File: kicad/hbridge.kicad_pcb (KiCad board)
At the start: 2 copper layers, 50 x 50 mm, 33 parts, among them P1 CONN_01X01, P10 CONN_01X01, P11 CONN_01X02, P2 CONN_01X01, P3 CONN_01X01, P4 CONN_01X01, P5 CONN_01X01, P6 CONN_01X02, P7 CONN_01X01, P8 CONN_01X01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

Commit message: wip #1
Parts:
- C2, C4: footprint Capacitors_SMD:C_0805 -> Capacitors_Tantalum_SMD:TantalC_SizeB_EIA-3528_HandSoldering
- D1, D2: footprint Diodes_ThroughHole:Diode_DO-35_SOD27_Horizontal_RM10 -> Diodes_SMD:Diode-DO-214BA
- P11, P6: footprint Socket_Strips:Socket_Strip_Straight_1x02 -> Connect:AK300-2
- moved C4 63.1 mm to (144.8, 83.8), turned to 90 degrees
- moved P11 50.4 mm to (129.5, 53.3)
- moved C6 48.2 mm to (114.3, 50.8)
- moved C7 47.7 mm to (111.8, 53.3)
- moved P5 47.1 mm to (139.7, 96.5)
- moved P2 46.7 mm to (134.6, 96.5)
- moved P1 45.3 mm to (115.0, 95.0)
- moved P4 45.0 mm to (120.0, 95.0)
- moved P3 39.6 mm to (124.5, 91.4)
- moved P10 38.3 mm to (104.1, 58.4)
- moved C2 38.1 mm to (116.8, 76.2)
- moved C5 37.7 mm to (109.2, 58.4)
- moved U3 35.4 mm to (119.4, 55.9), turned to 180 degrees
- moved C3 30.4 mm to (120.0, 90.0), turned to 270 degrees
- moved R5 29.4 mm to (111.8, 55.9), turned to 90 degrees
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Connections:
- net /Half Bridge/GND renamed /Half Bridge 1/GND
- net /Half Bridge/OUT renamed /Half Bridge 2/OUT
- net /Half Bridge/VCC renamed /Half Bridge 1/VCC
- net /Half Bridge/VPP renamed /Half Bridge 1/VPP
- net /Half Bridge/~SD renamed /Half Bridge 1/~SD
- D1 pad 2: Net-(D1-Pad2) -> Net-(C2-Pad1)
- D2 pad 2: Net-(D2-Pad2) -> Net-(C4-Pad1)
- P2 pad 1: /Half Bridge/IN -> /Half Bridge 1/IN
- P5 pad 1: /Half Bridge/IN -> /Half Bridge 2/IN
- U1 pad 2: /Half Bridge/IN -> /Half Bridge 1/IN
- U1 pad 8: Net-(D1-Pad2) -> Net-(C2-Pad1)
- U2 pad 2: /Half Bridge/IN -> /Half Bridge 2/IN
- U2 pad 8: Net-(D2-Pad2) -> Net-(C4-Pad1)
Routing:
- net /Half Bridge 1/GND: track 0.00 -> 84.6 mm
- net /Half Bridge 1/VPP: track 0.00 -> 36.2 mm
- net /Current Sensor/IP+: track 0.00 -> 21.6 mm
- net /Half Bridge 1/~SD: track 0.00 -> 18.0 mm
- net /Half Bridge 2/OUT: track 0.00 -> 15.3 mm
- net Net-(Q2-Pad2): track 0.00 -> 12.8 mm
- net Net-(Q4-Pad2): track 0.00 -> 12.8 mm
- net /Current Sensor/IP-: track 0.00 -> 9.32 mm
- net Net-(Q3-Pad2): track 0.00 -> 6.67 mm
- net Net-(Q1-Pad2): track 0.00 -> 6.67 mm
- net Net-(R4-Pad2): track 0.00 -> 4.93 mm
- net Net-(R3-Pad2): track 0.00 -> 4.93 mm

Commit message: initial place & route
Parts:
- P6: moved to B.Cu
- moved P8 44.1 mm to (113.0, 96.5)
- moved P9 43.2 mm to (108.0, 96.5)
- moved P7 40.8 mm to (102.9, 96.5)
- moved P10 40.6 mm to (118.1, 96.5)
- moved C7 38.3 mm to (115.6, 91.4), turned to 180 degrees
- moved R6 36.7 mm to (105.4, 91.4), turned to 0 degrees
- moved R5 32.7 mm to (119.4, 87.6)
- moved C3 23.5 mm to (143.5, 89.4), turned to 0 degrees
- moved P3 18.5 mm to (142.2, 96.5)
- moved P6 15.2 mm to (109.0, 53.6), turned to 180 degrees
- moved C2 15.2 mm to (131.8, 78.5)
- moved C1 15.0 mm to (131.8, 89.4), turned to 0 degrees
- moved C5 12.8 mm to (121.4, 54.6), turned to 90 degrees
- moved P4 12.2 mm to (132.1, 96.5)
- moved P1 12.1 mm to (127.0, 96.5)
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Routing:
- net /Current Sensor/~FAULT: track 0.00 -> 67.2 mm
- net GNDA: track 0.00 -> 64.8 mm
- net /Current Sensor/AVCC: track 0.00 -> 62.9 mm, vias 0 -> 1
- net Net-(R5-Pad2): track 0.00 -> 36.5 mm
- net /Half Bridge 1/VCC: track 0.00 -> 34.1 mm
- net /Half Bridge 1/GND: track 84.6 -> 64.5 mm
- net /Half Bridge 2/OUT: track 15.3 -> 33.6 mm
- net /Half Bridge 1/IN: track 0.00 -> 16.7 mm
- net /Half Bridge 2/IN: track 0.00 -> 16.3 mm
- net /Current Sensor/VOUT: track 0.00 -> 10.7 mm
- net /Current Sensor/IP+: track 21.6 -> 32.1 mm
- net Net-(C4-Pad1): track 0.00 -> 7.06 mm
- net Net-(Q2-Pad2): track 12.8 -> 5.77 mm
- net Net-(Q4-Pad2): track 12.8 -> 5.80 mm
- net Net-(C2-Pad1): track 0.00 -> 6.84 mm
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
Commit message: PCB good
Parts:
- moved R6 15.9 mm to (121.3, 91.4)
- moved P7 14.0 mm to (116.8, 96.5)
- moved P9 14.0 mm to (121.9, 96.5)
- moved R5 7.62 mm to (111.8, 87.6)
- moved P10 6.35 mm to (111.8, 96.5)
- moved P8 6.35 mm to (106.7, 96.5)
- moved P2 5.08 mm to (132.1, 96.5)
- moved P4 5.08 mm to (137.2, 96.5)
- moved C7 4.81 mm to (110.8, 91.4)
- moved C3 4.34 mm to (145.0, 93.5)
- moved U1 4.33 mm to (132.7, 88.1)
- moved U2 4.32 mm to (144.4, 88.1)
- moved C1 4.07 mm to (132.1, 93.5)
- moved R3 3.95 mm to (140.7, 77.5)
- moved C4 3.39 mm to (143.8, 81.3)
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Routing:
- net GNDA: track 64.8 -> 0.63 mm
- net /Half Bridge 1/GND: track 64.5 -> 19.4 mm, vias 0 -> 1
- net /Half Bridge 1/VPP: track 38.6 -> 0.00 mm
- net /Current Sensor/~FAULT: track 67.2 -> 50.4 mm
- net /Half Bridge 1/~SD: track 11.2 -> 22.6 mm
- net /Half Bridge 1/IN: track 16.7 -> 5.68 mm
- net Net-(R2-Pad2): track 0.00 -> 10.6 mm
- net /Current Sensor/IP-: track 8.78 -> 0.18 mm
- net Net-(Q1-Pad2): track 11.1 -> 19.3 mm
- net Net-(R5-Pad2): track 36.5 -> 43.7 mm
- net Net-(Q3-Pad2): track 11.1 -> 18.1 mm
- net /Current Sensor/AVCC: track 62.9 -> 59.4 mm
- net /Half Bridge 2/OUT: track 33.6 -> 30.2 mm
- net Net-(C4-Pad1): track 7.06 -> 10.3 mm
- net Net-(C2-Pad1): track 6.84 -> 10.0 mm
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- added copper zone on F.Cu, net /Current Sensor/IP+
- added copper zone on F.Cu, net /Current Sensor/IP-
- added copper zone on B.Cu, net /Half Bridge 1/GND
- added copper zone on B.Cu, net /Half Bridge 1/VPP
- added copper zone on F.Cu, net /Half Bridge 2/OUT
- added copper zone on F.Cu, net GNDA
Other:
- net class power added: clearance 0.2, trace_width 0.75, via_dia 1, via_drill 0.8

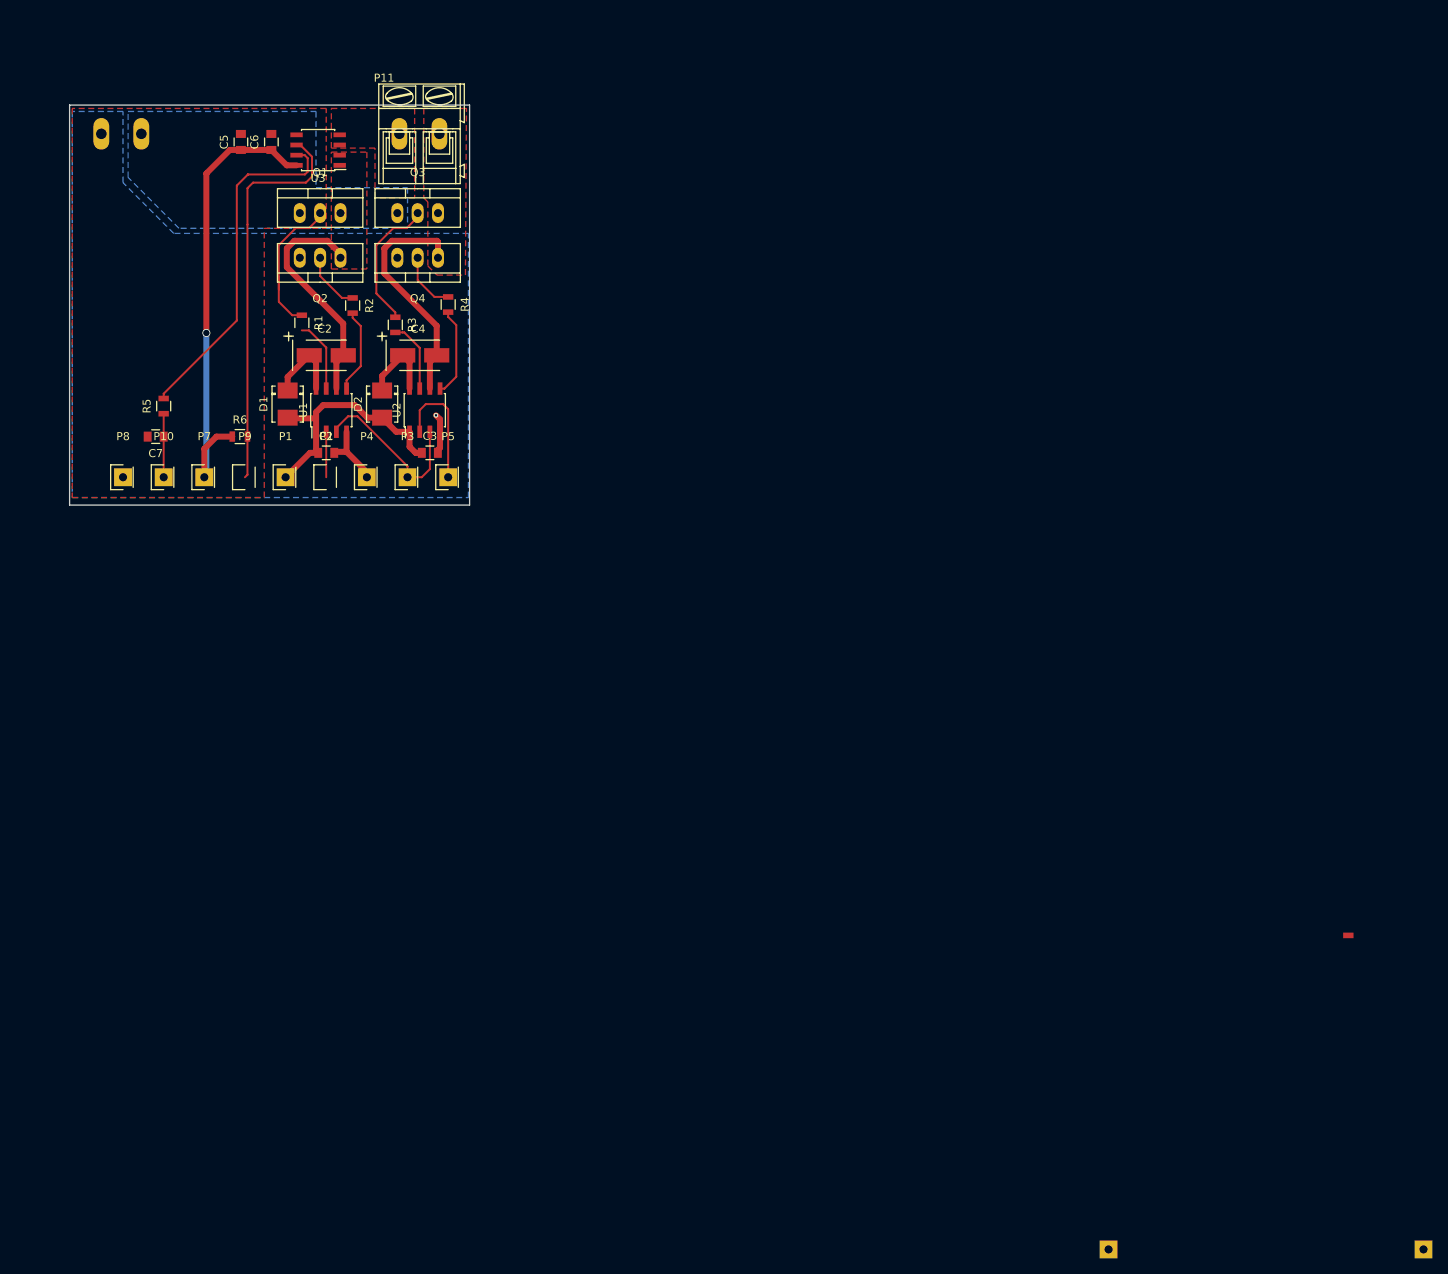
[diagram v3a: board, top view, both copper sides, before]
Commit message: add big cap for vpp
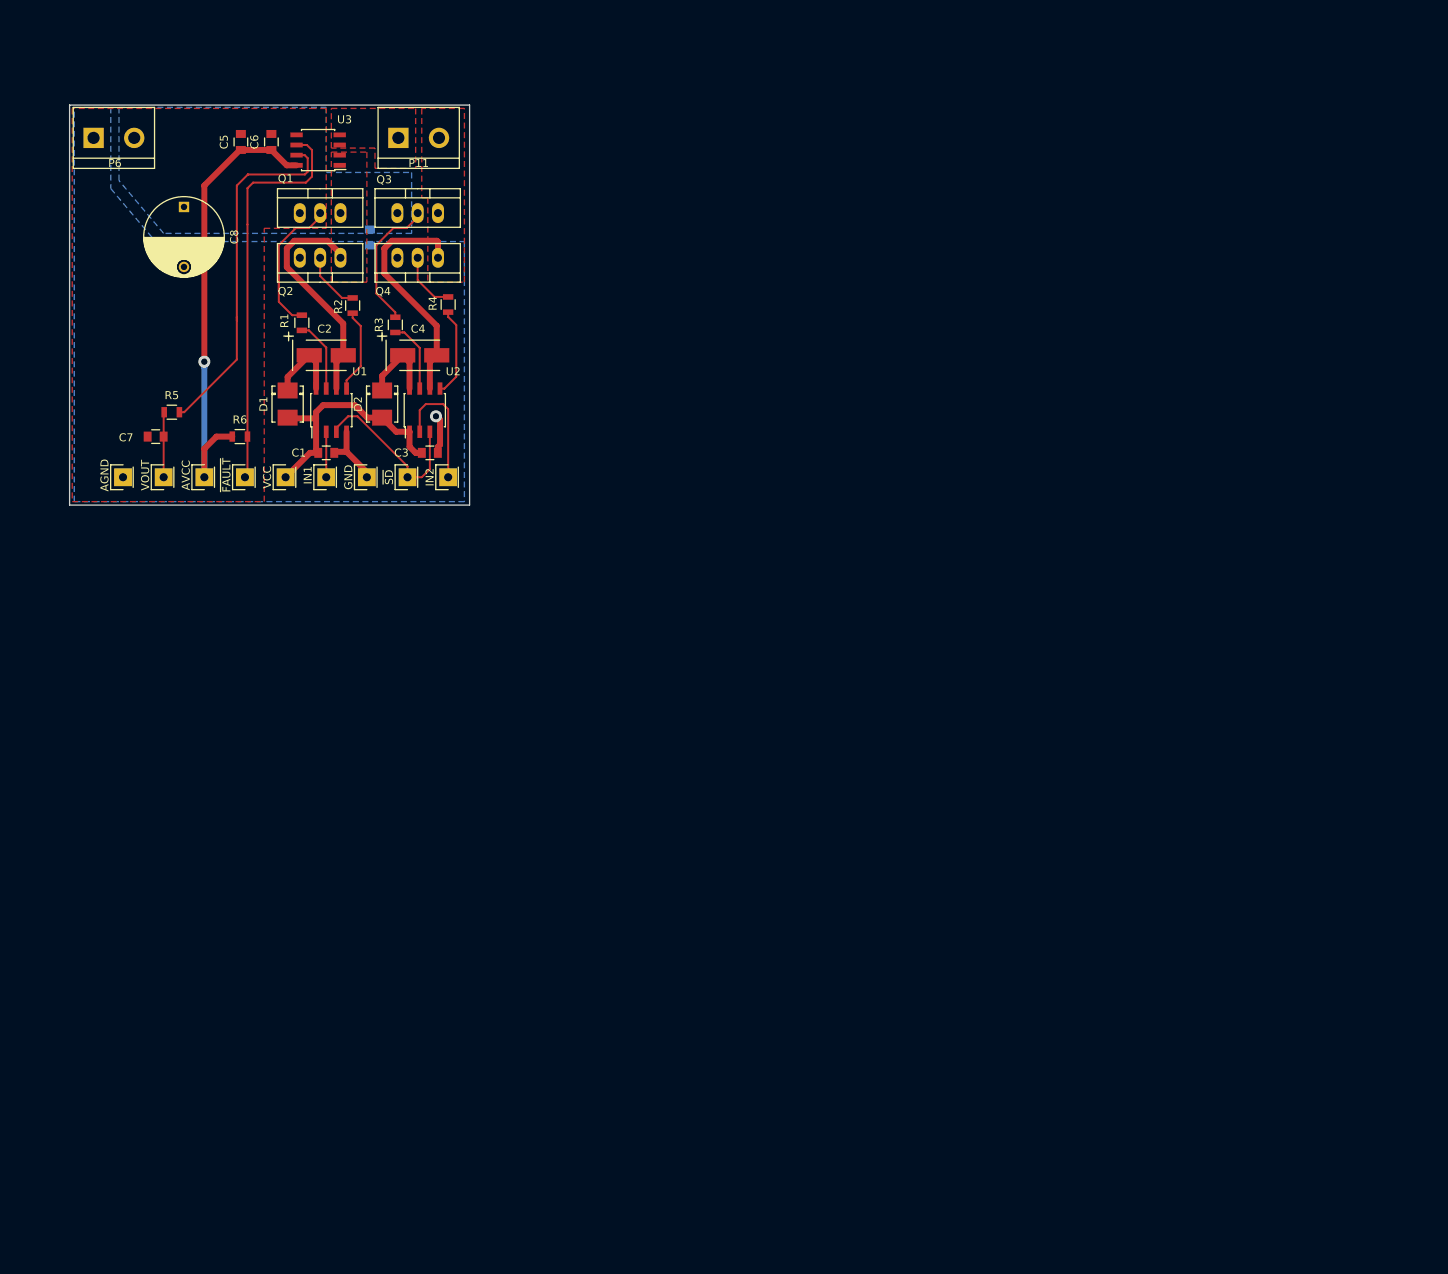
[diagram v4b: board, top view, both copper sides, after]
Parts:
- added C8: CP, Capacitors_ThroughHole:C_Radial_D10_L20_P7.5, F.Cu at (114.3, 62.7)
- added C9: C, Capacitors_SMD:C_0805, B.Cu at (137.5, 66.5)
- P1: value CONN_01X01 -> VCC
- P10: value CONN_01X01 -> VOUT
- P11: value CONN_01X02 -> OUT; footprint Connect:AK300-2 -> Connect:bornier2
- P2: value CONN_01X01 -> IN1
- P3: value CONN_01X01 -> ~SD
- P4: value CONN_01X01 -> GND
- P5: value CONN_01X01 -> IN2
- P6: value CONN_01X02 -> POWER; footprint Connect:AK300-2 -> Connect:bornier2; moved to F.Cu
- P7: value CONN_01X01 -> AVCC
- P8: value CONN_01X01 -> AGND
- P9: value CONN_01X01 -> ~FAULT
- moved P6 3.47 mm to (105.5, 54.1), turned to 0 degrees
- moved P11 2.47 mm to (143.6, 54.1)
- moved R5 1.27 mm to (112.8, 88.4), turned to 0 degrees
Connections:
- net /Half Bridge 1/VCC renamed /Half Bridge/VCC
- net /Half Bridge 1/~SD renamed /Half Bridge/~SD
- net /Half Bridge 2/OUT renamed /Half Bridge/OUT
- C1 pad 2: /Half Bridge 1/GND -> /Half Bridge/GND
- C3 pad 2: /Half Bridge 1/GND -> /Half Bridge/GND
- P2 pad 1: /Half Bridge 1/IN -> /Half Bridge/IN
- P4 pad 1: /Half Bridge 1/GND -> /Half Bridge/GND
- P5 pad 1: /Half Bridge 2/IN -> /Half Bridge/IN
- P6 pad 1: /Half Bridge 1/VPP -> /Half Bridge/GND
- P6 pad 2: /Half Bridge 1/GND -> /Half Bridge/VPP
- Q1 pad 1: /Half Bridge 1/VPP -> /Half Bridge/VPP
- Q2 pad 3: /Half Bridge 1/GND -> /Half Bridge/GND
- Q3 pad 1: /Half Bridge 1/VPP -> /Half Bridge/VPP
- Q4 pad 3: /Half Bridge 1/GND -> /Half Bridge/GND
- U1 pad 2: /Half Bridge 1/IN -> /Half Bridge/IN
- U1 pad 4: /Half Bridge 1/GND -> /Half Bridge/GND
- U2 pad 2: /Half Bridge 2/IN -> /Half Bridge/IN
- U2 pad 4: /Half Bridge 1/GND -> /Half Bridge/GND
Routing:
- net /Half Bridge/IN: track 0.00 -> 21.0 mm
- net /Half Bridge 1/GND: track 19.4 -> 0.00 mm, vias 1 -> 0
- net /Half Bridge 2/IN: track 15.3 -> 0.00 mm
- net /Half Bridge/GND: track 0.00 -> 14.7 mm, vias 0 -> 1
- net /Half Bridge 1/IN: track 5.68 -> 0.00 mm
- net Net-(R5-Pad2): track 43.7 -> 45.4 mm
- added copper zone on B.Cu, net /Half Bridge/GND
- added copper zone on B.Cu, net /Half Bridge/VPP
- removed copper zone on B.Cu, net /Half Bridge 1/GND
- removed copper zone on B.Cu, net /Half Bridge 1/VPP
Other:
- net class power: via_dia 1 -> 1.5
